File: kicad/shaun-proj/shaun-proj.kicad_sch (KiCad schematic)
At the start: 1 part

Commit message: 9v usb req
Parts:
- added C1: 1u, symbol Device:C
- added J1: USB_C_Receptacle_PowerOnly_6P, symbol Connector:USB_C_Receptacle_PowerOnly_6P
- added Q1: AO3401A, Package_TO_SOT_SMD:SOT-23, symbol Transistor_FET:AO3401A
- added R2: 1k, symbol Device:R_US
- added R3: 1M, Resistor_SMD:R_0603_1608Metric, symbol Device:R_US
- added U1: CH224K, Package_SO:SSOP-10-1EP_3.9x4.9mm_P1mm_EP2.1x3.3mm, symbol Interface_USB:CH224K
- R1: value R_US -> 6.8K; footprint (none) -> Resistor_SMD:R_0603_1608Metric
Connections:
- net GND: now reaches R1.1
- net GND: now also C1.2, J1.A12 (GND), J1.B12 (GND), U1.11 (GND)
- net at R1.2: now also U1.9 (CFG1)
- new net: C1.1, R2.1, U1.1 (VDD)
- new net: U1.4 (DP), U1.5 (DM)
- new net: J1.B5 (CC2), U1.6 (CC2)
- new net: J1.A5 (CC1), U1.7 (CC1)
- new net HV: Q1.3 (D)
- new net PG: Q1.1 (G), R3.2, U1.10 (PG)
- new net VBUS: J1.A9 (VBUS), J1.B9 (VBUS), Q1.2 (S), R2.2, R3.1
- no-connect marks 0 -> 3
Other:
- note added: ""Power Good" - maybe attach a resistor + LED here"
- note added: "1%"
- note added: "DP/DM not needed as only USB PD is used."
- note added: "No need to connect VBUS using USB PD only (CH224K)"
- note added: "This CH224K has been configured to operate like a CH221K. Unfortunately the CH221K isn't available on JLCPCB."

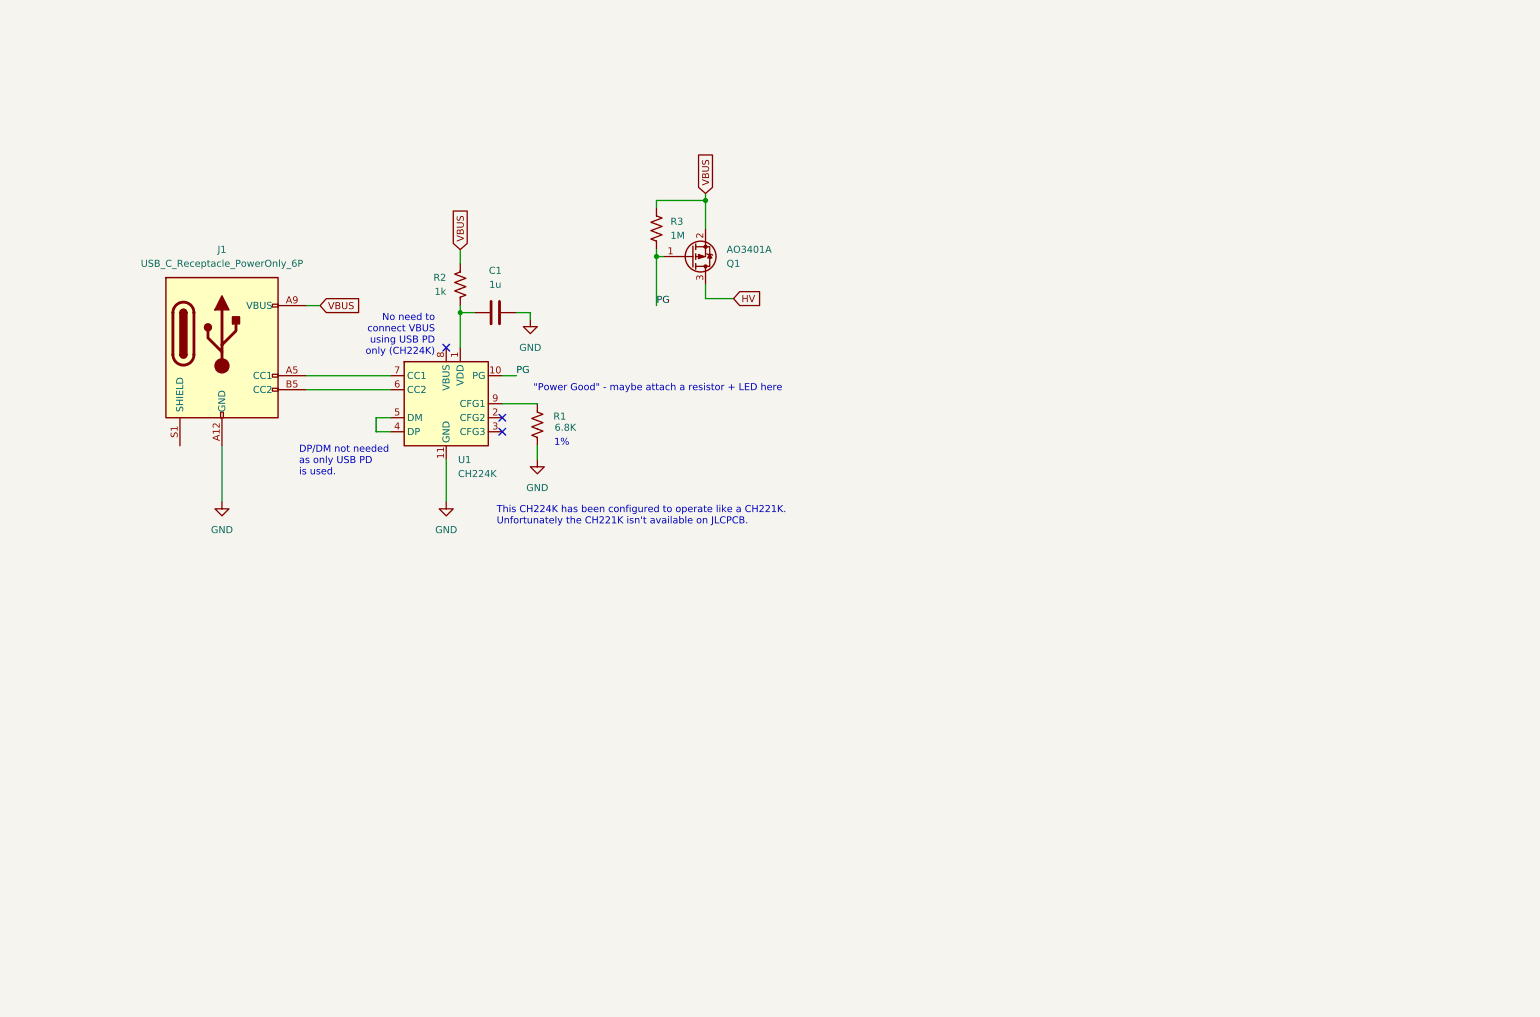
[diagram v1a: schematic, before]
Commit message: finish 1st draft of battery charging imlementation
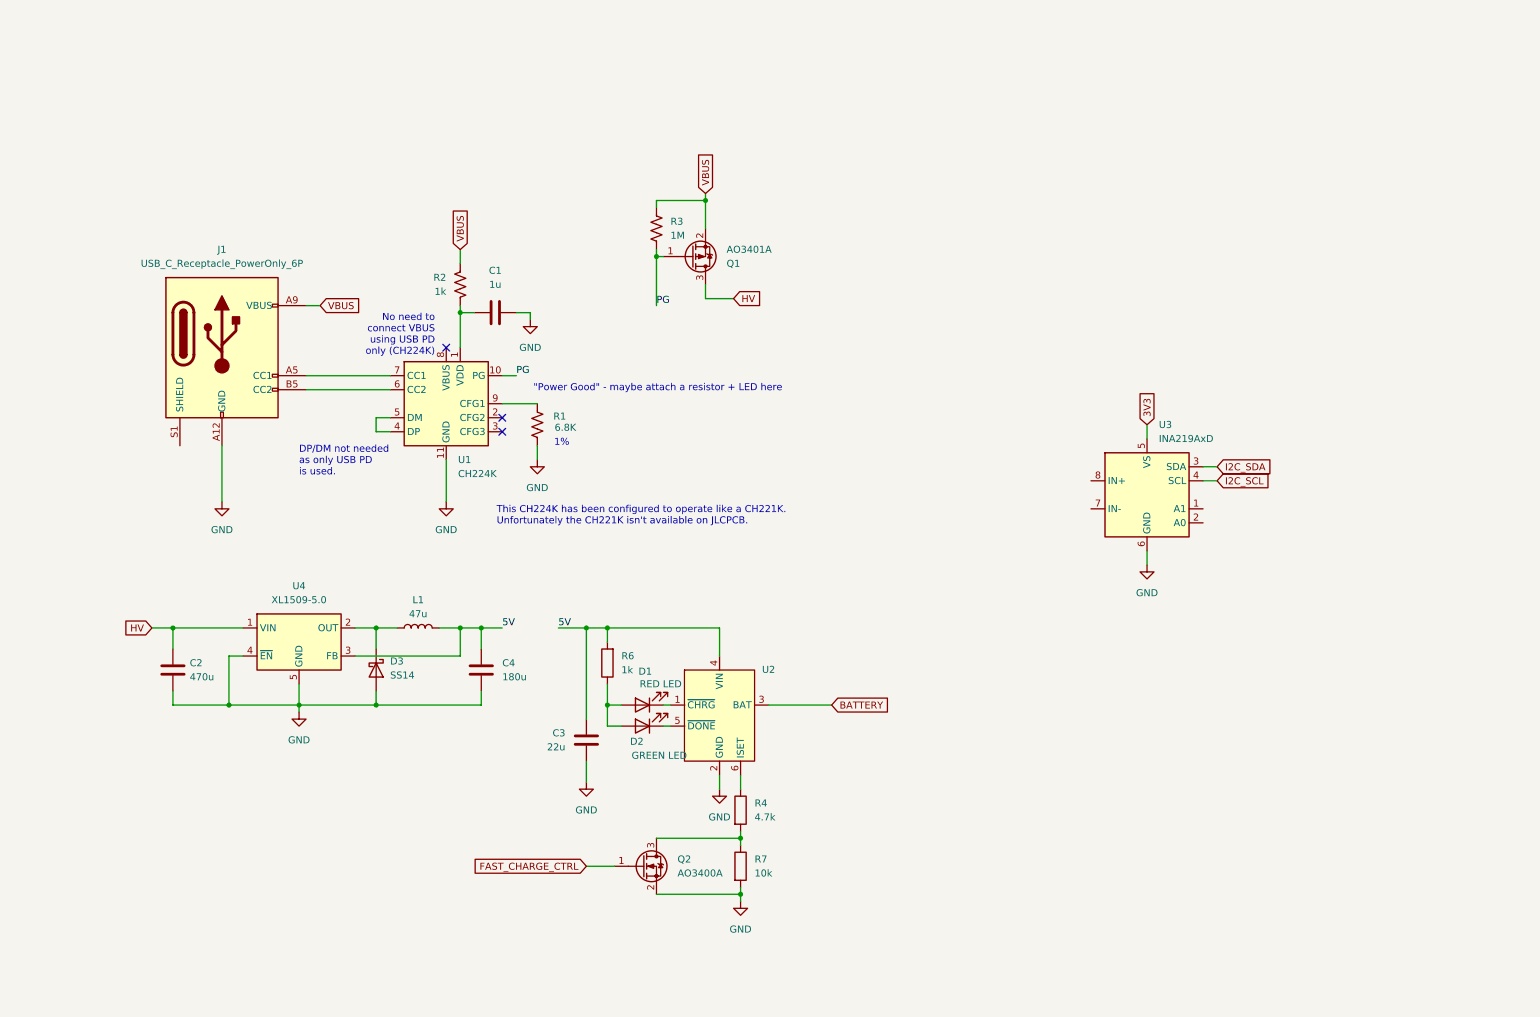
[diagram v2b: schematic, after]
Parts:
- added C2: 470u, symbol Device:C
- added C3: 22u, symbol Device:C
- added C4: 180u, symbol Device:C
- added D1: RED LED, symbol Device:LED
- added D2: GREEN LED, symbol Device:LED
- added D3: SS14, Diode_SMD:D_SMA, symbol Diode:SS14
- added L1: 47u, symbol Device:L
- added Q2: AO3400A, Package_TO_SOT_SMD:SOT-23, symbol Transistor_FET:AO3400A
- added R4: 4.7k, symbol Device:R
- added R6: 1k, symbol Device:R
- added R7: 10k, symbol Device:R
- added U2: ~, symbol CustomSymbols:FM4057S42
- added U3: INA219AxD, Package_SO:SOIC-8_3.9x4.9mm_P1.27mm, symbol Sensor_Energy:INA219AxD
- added U4: XL1509-5.0, Package_SO:SOIC-8_3.9x4.9mm_P1.27mm, symbol Regulator_Switching:XL1509-5.0
- J1: footprint (none) -> Connector_USB:USB_C_Receptacle_HRO_TYPE-C-31-M-17; JLC (none) -> https://jlcpcb.com/partdetail/ShouHan-TYPE_C_6P_073/C668623
- U1: JLC (none) -> https://jlcpcb.com/partdetail/wch_jiangsu_Qin_heng-CH224K/C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
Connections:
- net GND: now also C2.2, C3.2, C4.2, D3.2 (A), Q2.2 (S), R7.2, U2.2 (GND), U3.6 (GND), U4.4 (~{EN}), U4.5 (GND), U4.6 (GND), U4.7 (GND), U4.8 (GND)
- net HV: now also C2.1, U4.1 (VIN)
- new net: D3.1 (K), L1.1, U4.2 (OUT)
- new net: R4.1, U2.6 (ISET)
- new net: Q2.3 (D), R4.2, R7.1
- new net: D1.1 (K), U2.1 (~{CHRG})
- new net: D1.2 (A), D2.2 (A), R6.1
- new net: D2.1 (K), U2.5 (~{DONE})
- new net 3V3: U3.5 (VS)
- new net 5V: C3.1, C4.1, L1.2, R6.2, U2.4 (VIN), U4.3 (FB)
- new net BATTERY: U2.3 (BAT)
- new net FAST_CHARGE_CTRL: Q2.1 (G)
- new net I2C_SCL: U3.4 (SCL)
- new net I2C_SDA: U3.3 (SDA)

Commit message: improve battery charging circuit greatly, start with battery output monitoring
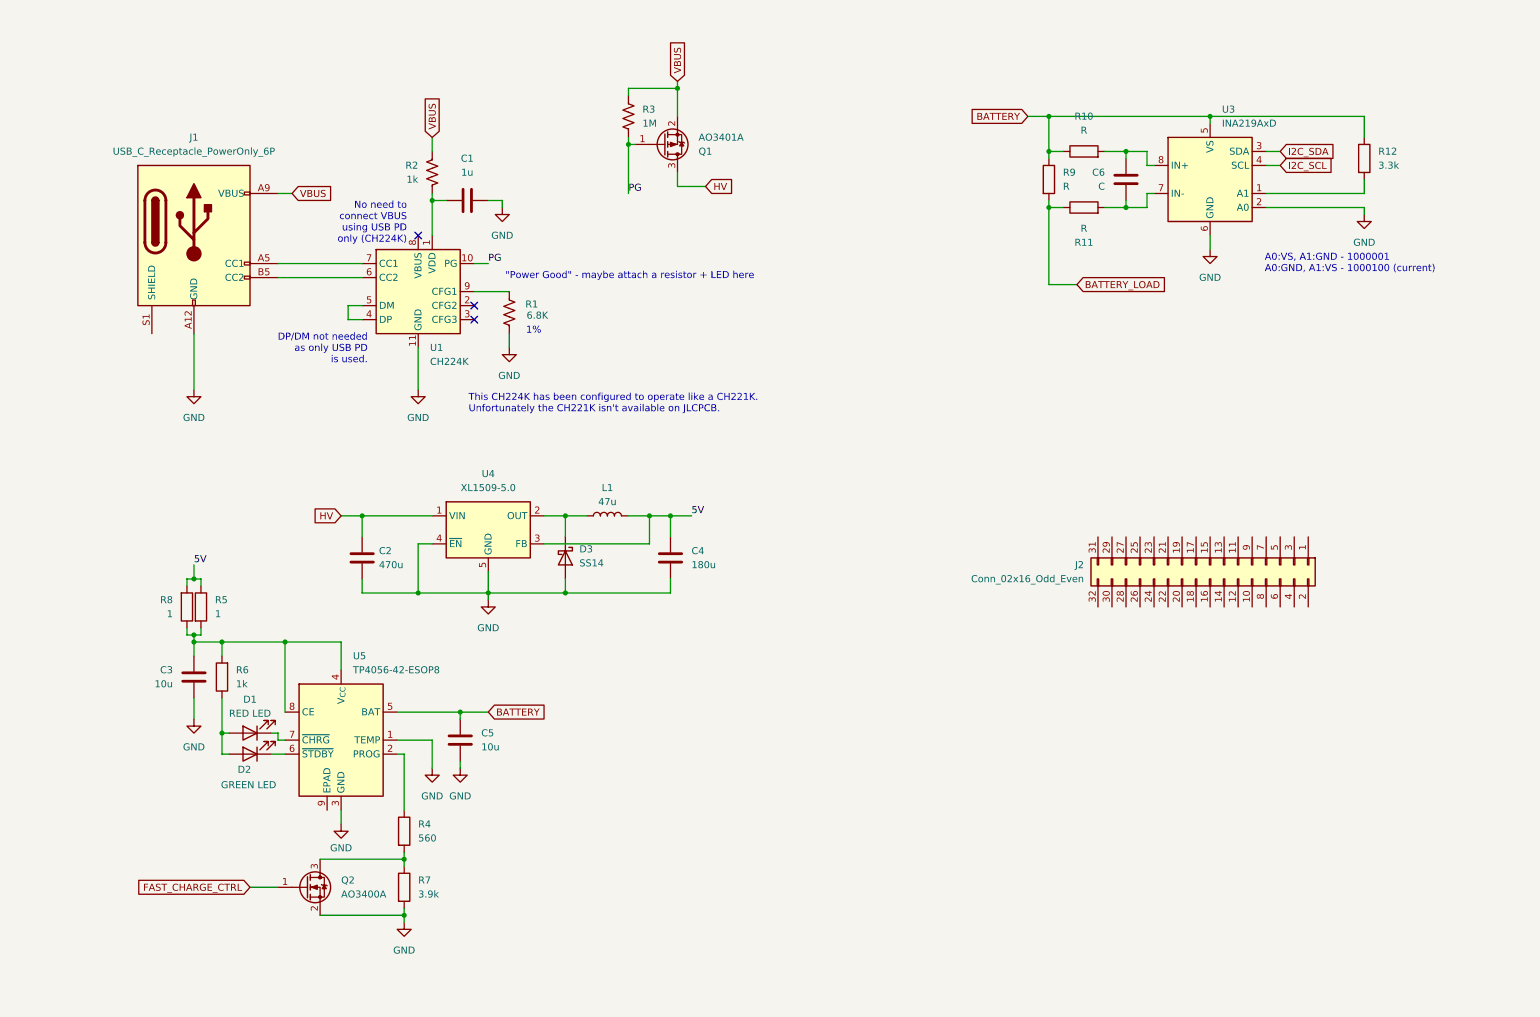
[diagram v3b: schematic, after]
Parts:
- removed U2: ~, symbol CustomSymbols:FM4057S42
- added C5: 10u, symbol Device:C
- added C6: C, symbol Device:C
- added J2: Conn_02x16_Odd_Even, symbol Connector_Generic:Conn_02x16_Odd_Even
- added R10, R11, R9: R, symbol Device:R
- added R12: 3.3k, Resistor_SMD:R_0603_1608Metric, symbol Device:R
- added R5, R8: 1, symbol Device:R
- added U5: TP4056-42-ESOP8, Package_SO:SOIC-8-1EP_3.9x4.9mm_P1.27mm_EP2.41x3.3mm_ThermalVias, symbol Battery_Management:TP4056-42-ESOP8
- C3: value 22u -> 10u
- R4: value 4.7k -> 560; footprint (none) -> Resistor_SMD:R_0603_1608Metric
- R6: footprint (none) -> Resistor_SMD:R_0603_1608Metric
- R7: value 10k -> 3.9k; footprint (none) -> Resistor_SMD:R_0603_1608Metric
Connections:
- net 3V3 is gone; now on net BATTERY: U3.5 (VS)
- net 5V: now also R5.1, R8.2; no longer C3.1, R6.2
- net BATTERY: now also C5.1, R10.1, R12.1, R9.1, U5.5 (BAT)
- net GND: now also U3.2 (A0), C5.2, U5.1 (TEMP), U5.3 (GND)
- net at R4.1: now also U5.2 (PROG)
- net at U3.1 (A1): now also R12.2
- net at U3.7 (IN-): now also C6.1, R11.2
- net at U3.8 (IN+): now also C6.2, R10.2
- net at D1.1 (K): now also U5.7 (~{CHRG})
- net at D2.1 (K): now also U5.6 (~{STDBY})
- new net: C3.1, R5.2, R6.2, R8.1, U5.4 (V_{CC}), U5.8 (CE)
- new net BATTERY_LOAD: R11.1, R9.2
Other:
- note added: "A0:VS, A1:GND - 1000001 A0:GND, A1:VS - 1000100 (current)"
- moved on the sheet: C1, C2, C3, C4, D1, D2, D3, J1, L1, Q1, Q2, R1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

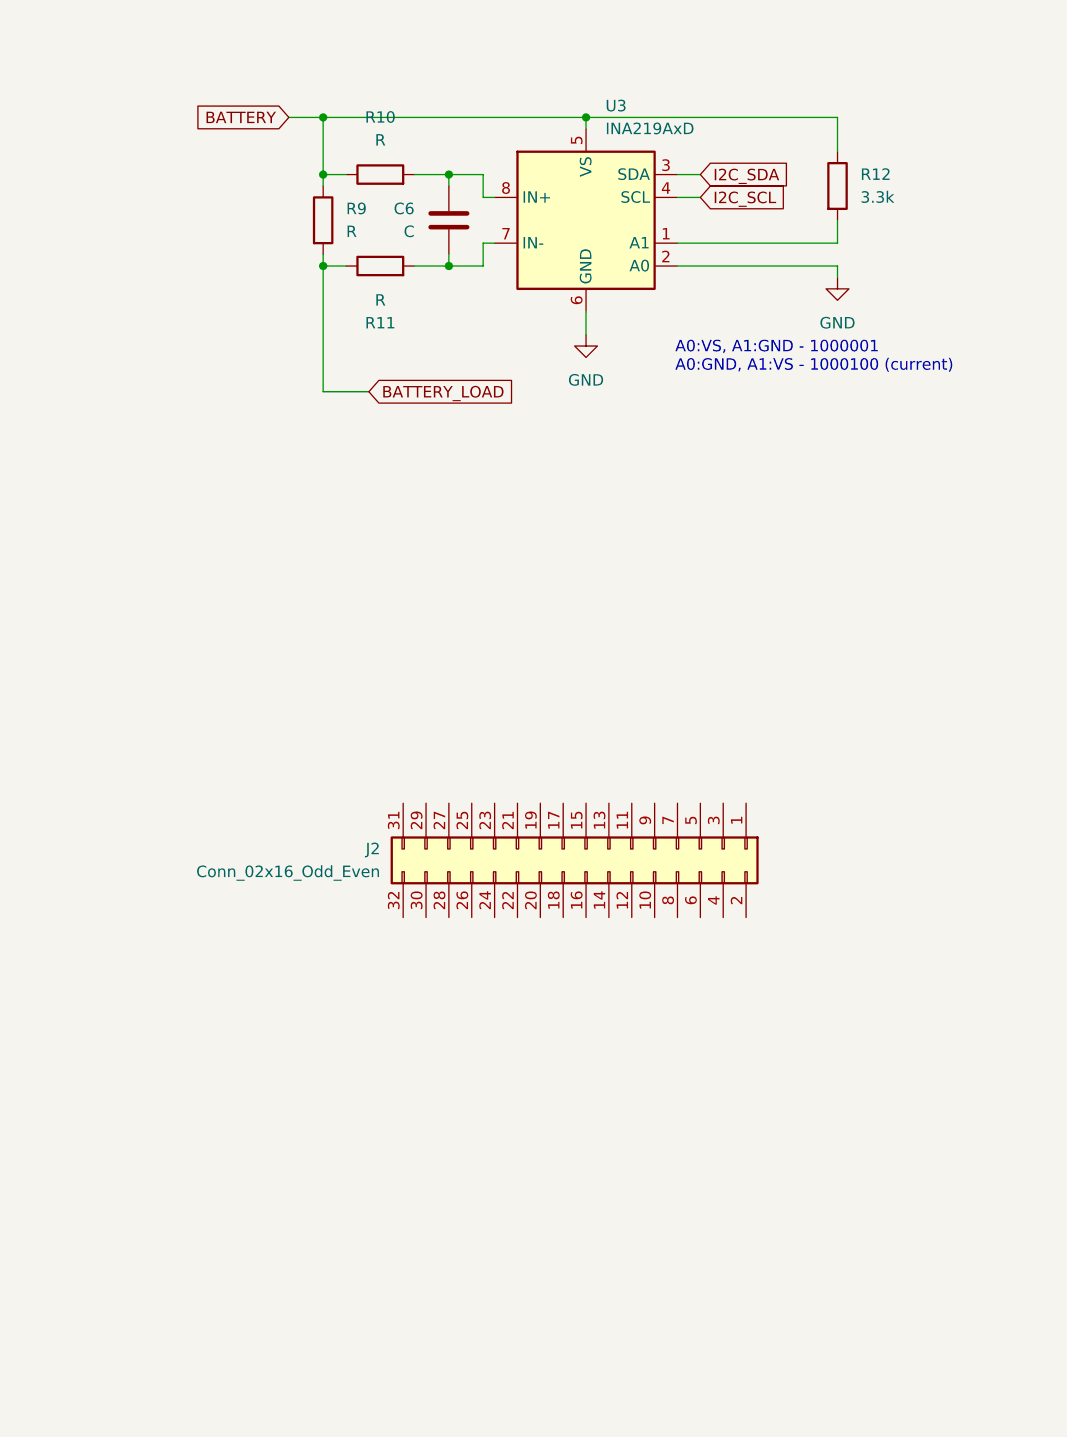
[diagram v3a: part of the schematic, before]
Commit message: add connectors and stuff
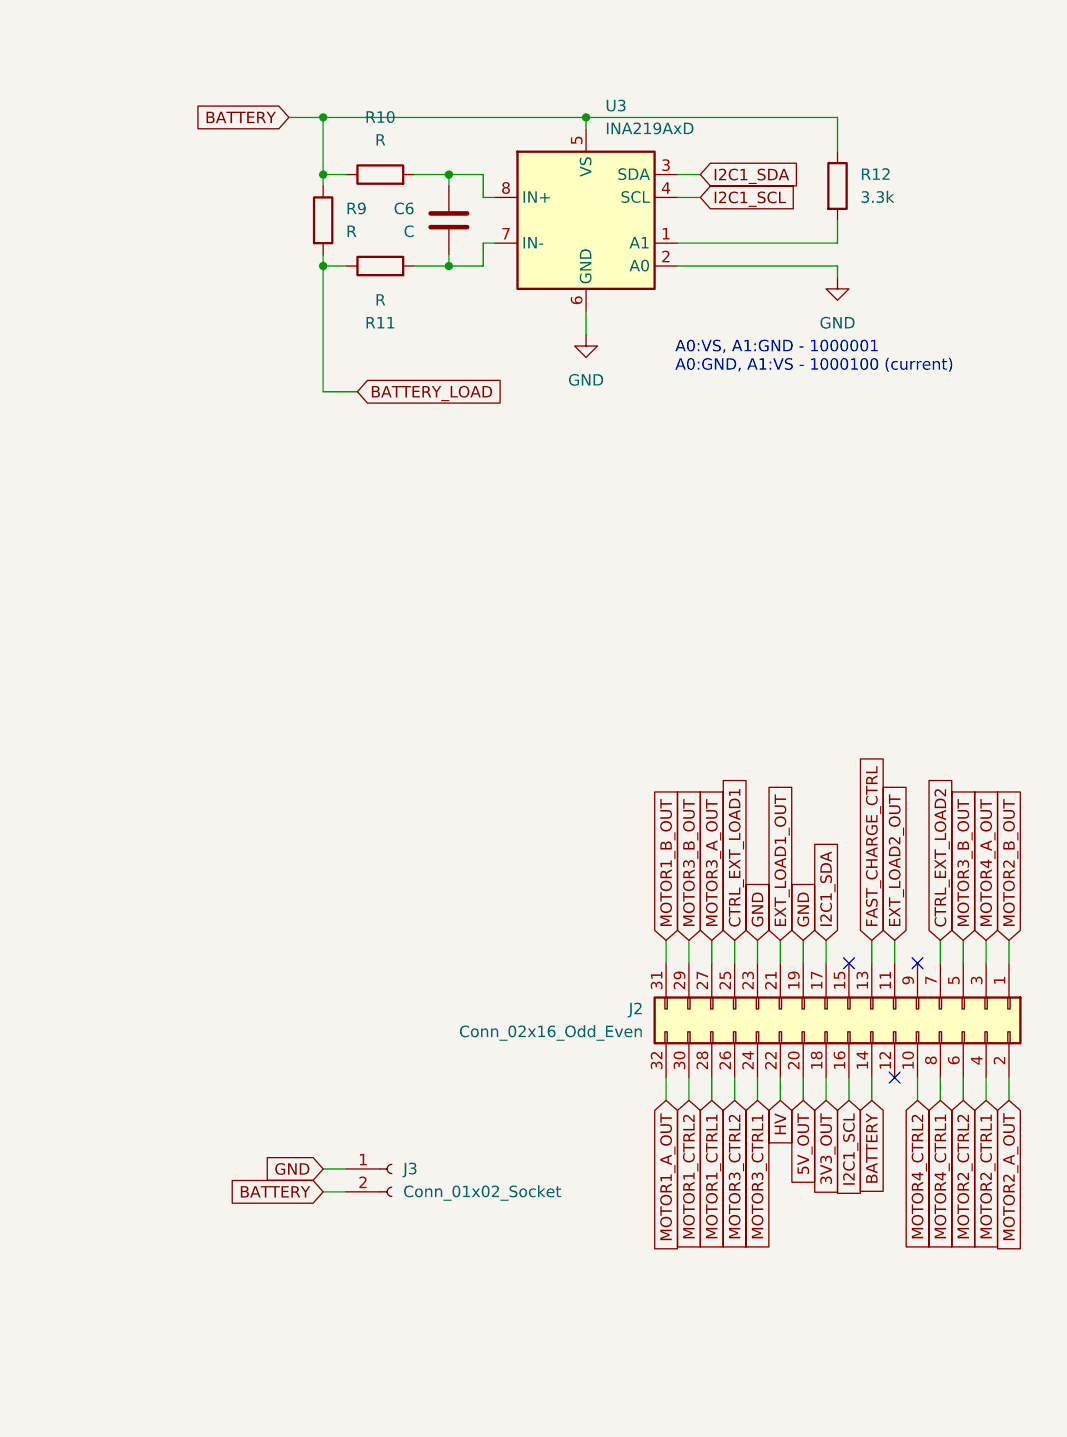
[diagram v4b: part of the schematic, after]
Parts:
- added J3: Conn_01x02_Socket, Connector_JST:JST_PH_S2B-PH-K_1x02_P2.00mm_Horizontal, symbol Connector:Conn_01x02_Socket
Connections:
- net I2C_SCL is gone; now on net I2C1_SCL: U3.4 (SCL)
- net I2C_SDA is gone; now on net I2C1_SDA: U3.3 (SDA)
- net BATTERY: now also J2.14 (Pin_14), J3.2 (Pin_2)
- net FAST_CHARGE_CTRL: now also J2.13 (Pin_13)
- net GND: now also J2.19 (Pin_19), J2.23 (Pin_23), J3.1 (Pin_1)
- net HV: now also J2.22 (Pin_22)
- net MOTOR2_B_OUT: now reaches J2.1 (Pin_1)
- net MOTOR4_CTRL2: now reaches J2.10 (Pin_10)
- net EXT_LOAD2_OUT: now reaches J2.11 (Pin_11)
- net I2C1_SCL: now reaches J2.16 (Pin_16)
- net I2C1_SDA: now reaches J2.17 (Pin_17)
- net 3V3_OUT: now reaches J2.18 (Pin_18)
- net MOTOR2_A_OUT: now reaches J2.2 (Pin_2)
- net 5V_OUT: now reaches J2.20 (Pin_20)
- net EXT_LOAD1_OUT: now reaches J2.21 (Pin_21)
- net MOTOR3_CTRL1: now reaches J2.24 (Pin_24)
- net CTRL_EXT_LOAD1: now reaches J2.25 (Pin_25)
- net MOTOR3_CTRL2: now reaches J2.26 (Pin_26)
- net MOTOR3_A_OUT: now reaches J2.27 (Pin_27)
- net MOTOR1_CTRL1: now reaches J2.28 (Pin_28)
- net MOTOR3_B_OUT: now reaches J2.29 (Pin_29)
- net MOTOR3_B_OUT: now also J2.5 (Pin_5)
- net MOTOR4_A_OUT: now reaches J2.3 (Pin_3)
- net MOTOR1_CTRL2: now reaches J2.30 (Pin_30)
- net MOTOR1_B_OUT: now reaches J2.31 (Pin_31)
- net MOTOR1_A_OUT: now reaches J2.32 (Pin_32)
- net MOTOR2_CTRL1: now reaches J2.4 (Pin_4)
- net MOTOR2_CTRL2: now reaches J2.6 (Pin_6)
- net CTRL_EXT_LOAD2: now reaches J2.7 (Pin_7)
- net MOTOR4_CTRL1: now reaches J2.8 (Pin_8)
- no-connect marks 3 -> 6
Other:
- moved on the sheet: J2
